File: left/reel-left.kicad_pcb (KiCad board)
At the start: 2 copper layers, 144 x 92 mm, 44 parts, among them J1 Conn_01x02, SW1 SW_Push, SW10 SW_Push, SW11 SW_Push, SW12 SW_Push, SW13 SW_Push, SW14 SW_Push, SW15 SW_Push, SW16 SW_Push, SW17 SW_Push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

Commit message: dit
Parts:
- moved SW21 26.3 mm to (216.4, 122.3)
- moved U1 0.99 mm to (172.0, 74.0)
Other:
- board size 144 x 92 mm -> 164 x 93.7 mm

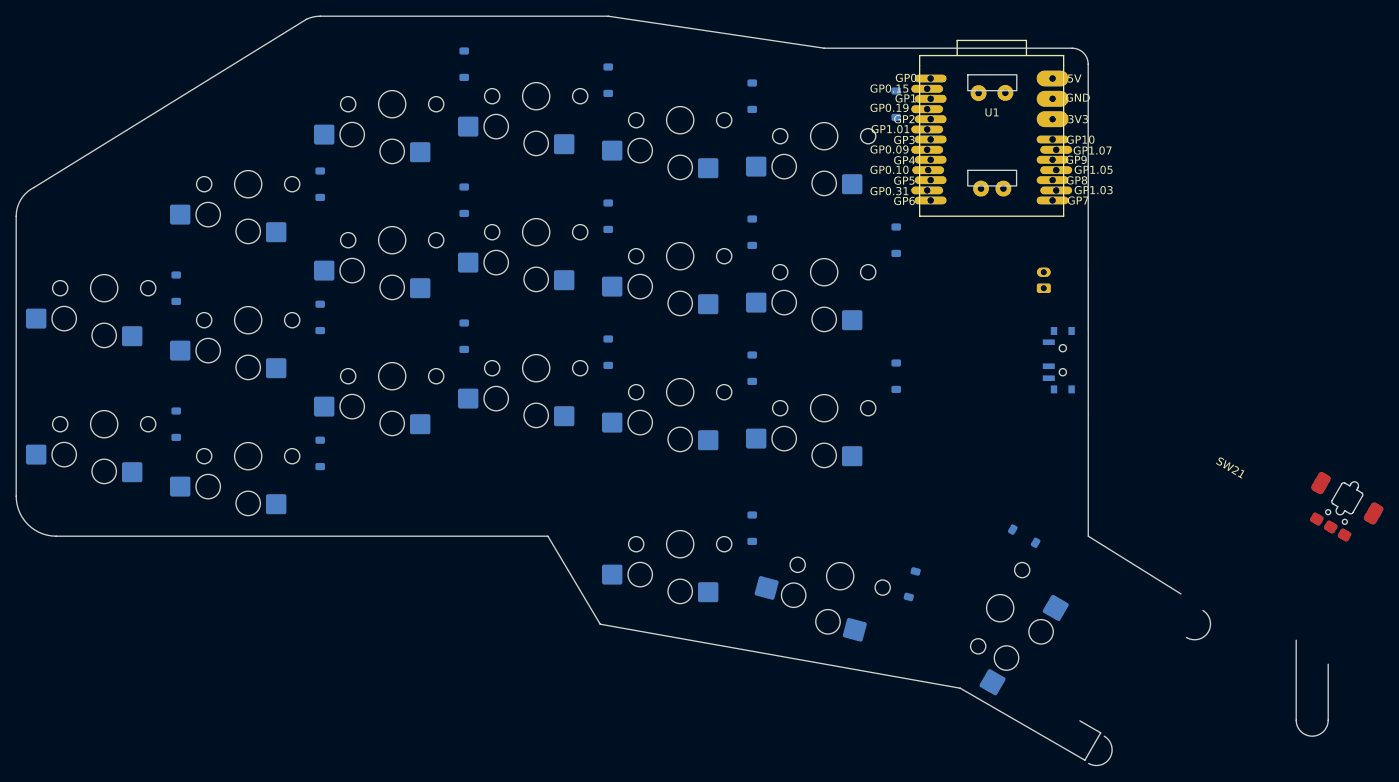
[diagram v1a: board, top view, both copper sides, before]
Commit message: Update left board encoder footprint
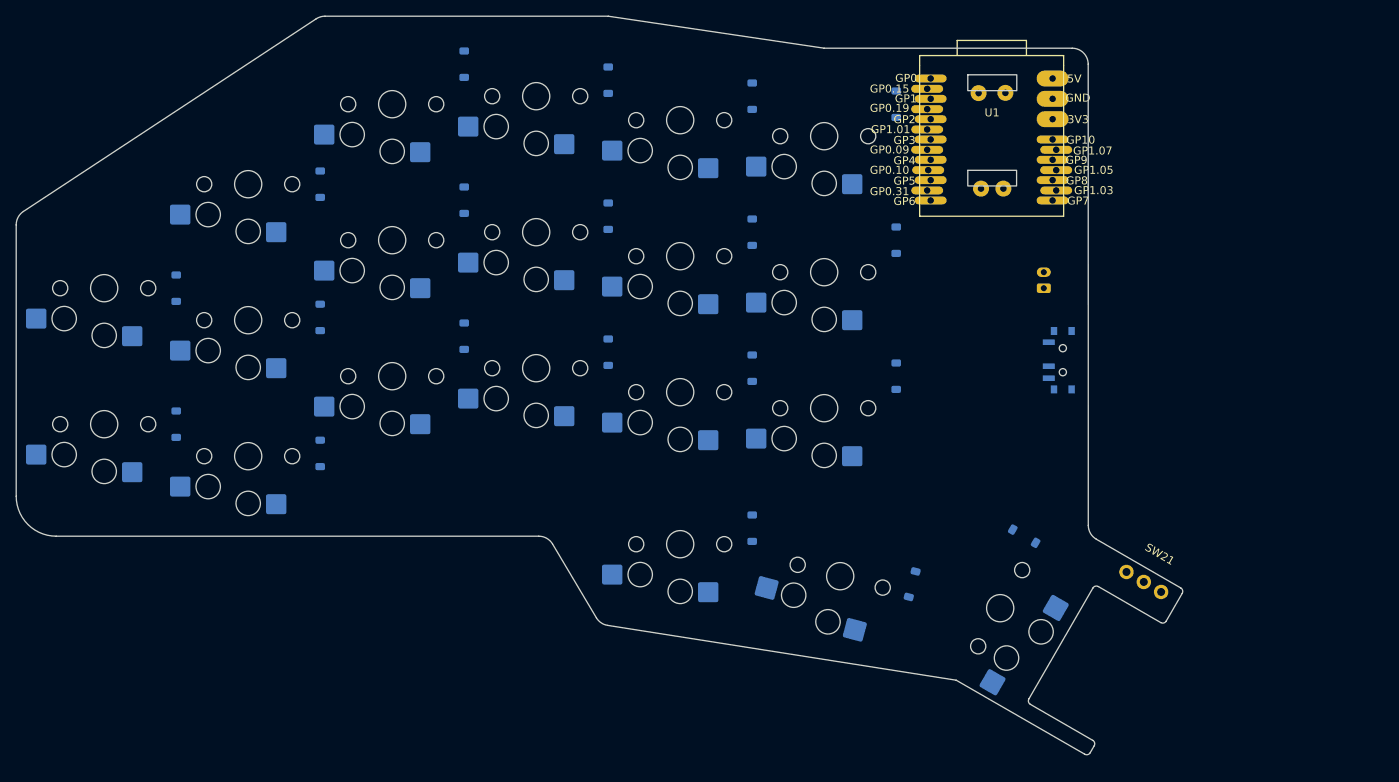
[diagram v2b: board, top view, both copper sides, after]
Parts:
- SW21: footprint reel:rotary_encoder_EC05E_Vert -> reel:RotaryEncoder_BM10_3Pin
- moved SW21 27.5 mm to (190.9, 132.7)
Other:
- board size 164 x 93.7 mm -> 145.8 x 92.3 mm

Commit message: Update left board assets
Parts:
- added Ref**: Val**, reel:m2_Spacer_Hole, F.Cu at (151.0, 71.0)
- added Ref**: Val**, reel:m2_Spacer_Hole, F.Cu at (165.0, 139.0)
- added Ref**: Val**, reel:m2_Spacer_Hole, F.Cu at (119.0, 122.0)
- added Ref**: Val**, reel:m2_Spacer_Hole, F.Cu at (85.0, 71.0)
- added Ref**: Val**, reel:m2_Spacer_Hole, F.Cu at (55.0, 122.0)
- moved D1 18.1 mm to (70.5, 78.5), turned to -90 degrees
- moved D16 18.1 mm to (52.5, 91.5), turned to -90 degrees
- moved D17 18.1 mm to (52.5, 108.5), turned to -90 degrees
- moved D18 18.0 mm to (124.0, 126.0), turned to -90 degrees
- moved D11 18.0 mm to (70.5, 112.5), turned to -90 degrees
- moved D6 18.0 mm to (70.5, 95.5), turned to -90 degrees
- moved D19 17.7 mm to (145.0, 128.0), turned to -105 degrees
- moved D13 17.7 mm to (106.5, 101.5), turned to -90 degrees
- moved D3 17.7 mm to (106.5, 67.5), turned to -90 degrees
- moved D8 17.7 mm to (106.5, 84.5), turned to -90 degrees
- moved D14 17.6 mm to (124.5, 104.5), turned to -90 degrees
- moved D4 17.6 mm to (124.5, 70.5), turned to -90 degrees
- moved D9 17.6 mm to (124.5, 87.5), turned to -90 degrees
- moved D10 17.5 mm to (142.5, 89.5), turned to -90 degrees
- moved D12 17.5 mm to (88.5, 102.5), turned to -90 degrees
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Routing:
- net Row3: track 0.00 -> 155.1 mm, vias 0 -> 4
- net Col1: track 0.00 -> 88.4 mm
- net Col4: track 0.00 -> 76.4 mm
- net Col3: track 0.00 -> 70.7 mm
- net Col2: track 0.00 -> 68.7 mm
- net Col0: track 0.00 -> 61.6 mm
- net Row0: track 0.00 -> 22.9 mm, vias 0 -> 2
- net Net-(D20-A): track 0.00 -> 21.0 mm
- net Net-(D9-A): track 0.00 -> 6.65 mm
- net Net-(D8-A): track 0.00 -> 6.65 mm
- net Net-(D7-A): track 0.00 -> 6.65 mm
- net Net-(D6-A): track 0.00 -> 6.65 mm
- net Net-(D5-A): track 0.00 -> 6.65 mm
- net Net-(D4-A): track 0.00 -> 6.65 mm
- net Net-(D3-A): track 0.00 -> 6.65 mm
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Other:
- board size 145.8 x 92.3 mm -> 146.2 x 93.3 mm
